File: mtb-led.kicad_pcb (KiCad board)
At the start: 2 copper layers, 120 x 50 mm, 60 parts, among them J7 AVR-ISP-6, J9 DEBUG, SW1 SW_Push, U1 ATmega328PB-A, U2 78M05, U3 TLC5940PWP, U4 TLC5940PWP, U5 MAX487E, Y1 14.7456 MHz

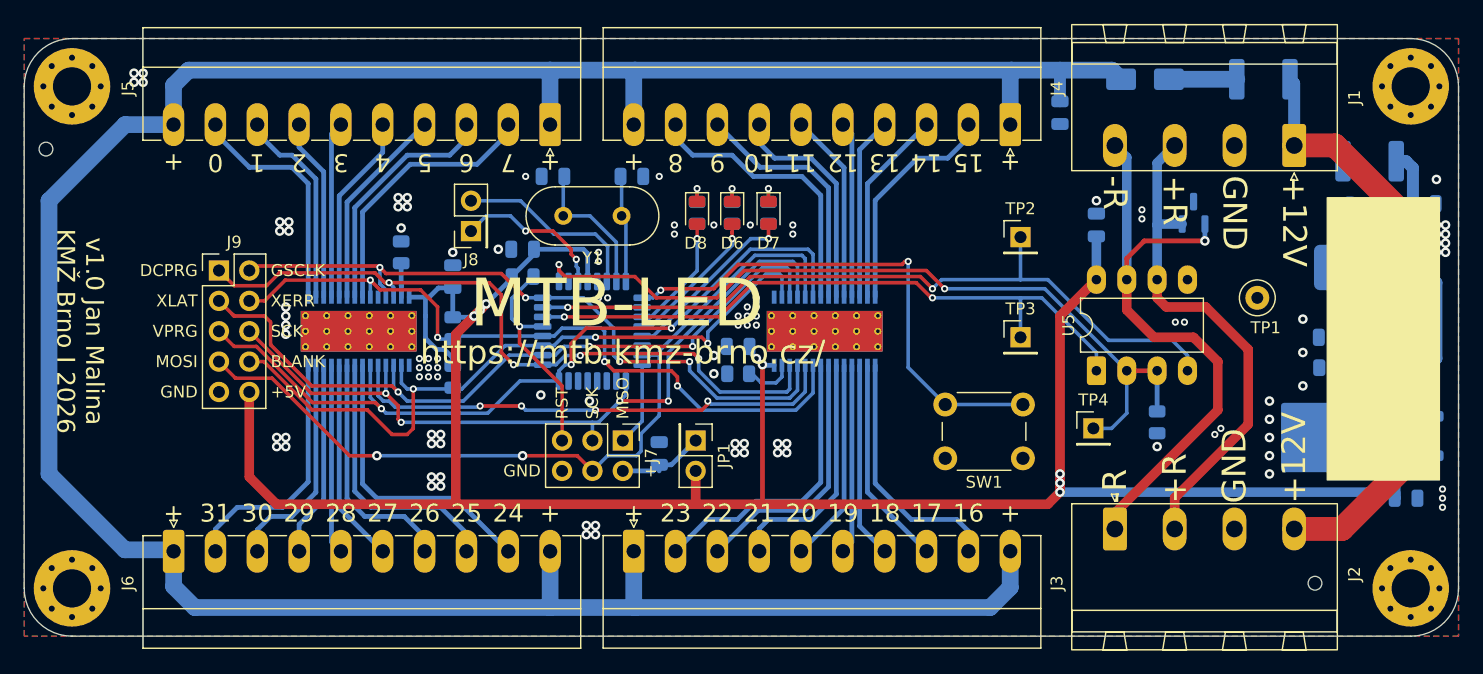
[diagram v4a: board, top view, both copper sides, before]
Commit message: Tweak silkscreen.
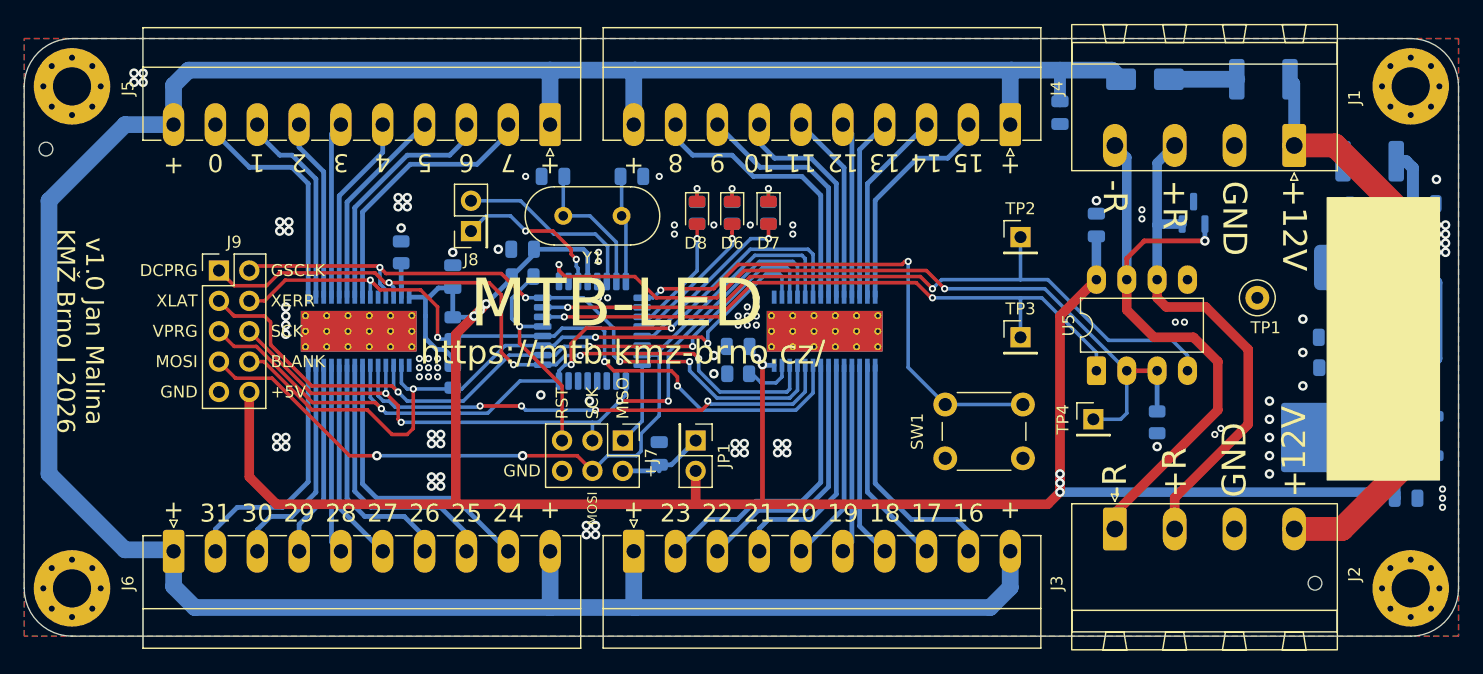
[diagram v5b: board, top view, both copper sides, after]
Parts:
- Y1: footprint Crystal:Crystal_HC49-U_Vertical -> Crystal:Crystal_HC49-4H_Vertical
- moved TP4 0.76 mm to (171.4, 101.9)
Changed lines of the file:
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@@
 	(footprint "Connector_PinHeader_2.54mm:PinHeader_1x01_P2.54mm_Vertical"
 		(layer "F.Cu")
-		(at 171.45 102.616)
+		(at 171.45 101.854)
 		(descr "Through hole straight pin header, 1x01, 2.54mm pitch, single row")
 		(tags "Through hole pin header THT 1x01 2.54mm single row")
 		(property "Reference" "TP4"
-			(at 0 -2.38 0)
+			(at -2.55 0 90)
 			(layer "F.SilkS")
 			(effects
@@
 		)
 	)
-	(footprint "Crystal:Crystal_HC49-U_Vertical"
+	(footprint "Crystal:Crystal_HC49-4H_Vertical"
 		(layer "F.Cu")
 		(at 131.98 84.836 180)
-		(descr "HC-49/U, Crystal, http://5hertz.com/pdfs/04404_D.pdf")
+		(descr "HC-49-4H, Crystal, http://5hertz.com/pdfs/04404_D.pdf")
 		(property "Reference" "Y1"
-			(at 2.44 -3.52 0)
+			(at 2.44 -3.52 180)
 			(layer "F.SilkS")
 			(effects
@@
 		)
 		(property "Value" "14.7456 MHz"
-			(at 2.44 3.52 0)
+			(at 2.44 3.52 180)
 			(layer "F.Fab")
 			(effects
@@
 		)
 		(property "Datasheet" ""
-			(at 0 0 0)
+			(at 0 0 180)
 			(layer "F.Fab")
 			(hide yes)
@@
 		)
 		(property "Description" "Two pin crystal"
-			(at 0 0 0)
+			(at 0 0 180)
 			(layer "F.Fab")
 			(hide yes)
@@
 		(attr through_hole)
 		(fp_line
-			(start 5.565 2.435)
-			(end -0.685 2.435)
+			(start 5.64 2.435)
+			(end -0.76 2.435)
 			(stroke
 				(width 0.12)
@@
 		)
 		(fp_line
-			(start -0.685 -2.435)
-			(end 5.565 -2.435)
+			(start -0.76 -2.435)
+			(end 5.64 -2.435)
 			(stroke
 				(width 0.12)
@@
 		)
 		(fp_arc
-			(start 5.565 -2.435)
-			(mid 8 0)
-			(end 5.565 2.435)
+			(start 5.64 -2.435)
+			(mid 8.075 0)
+			(end 5.64 2.435)
 			(stroke
 				(width 0.12)
@@
 		)
 		(fp_arc
-			(start -0.685 2.435)
-			(mid -3.12 0)
-			(end -0.685 -2.435)
+			(start -0.76 2.435)
+			(mid -3.195 0)
+			(end -0.76 -2.435)
 			(stroke
 				(width 0.12)
@@
 		)
 		(fp_line
-			(start 5.56 2.83)
-			(end -0.68 2.83)
+			(start 5.64 2.83)
+			(end -0.76 2.83)
 			(stroke
 				(width 0.05)
@@
 		)
 		(fp_line
-			(start -0.68 -2.83)
-			(end 5.56 -2.83)
+			(start -0.76 -2.83)
+			(end 5.64 -2.83)
 			(stroke
 				(width 0.05)
@@
 		)
 		(fp_arc
-			(start 5.56 -2.83)
-			(mid 8.39 0)
-			(end 5.56 2.83)
+			(start 5.64 -2.83)
+			(mid 8.47 0)
+			(end 5.64 2.83)
 			(stroke
 				(width 0.05)
@@
 		)
 		(fp_arc
-			(start -0.68 2.83)
-			(mid -3.51 0)
-			(end -0.68 -2.83)
+			(start -0.76 2.83)
+			(mid -3.59 0)
+			(end -0.76 -2.83)
 			(stroke
 				(width 0.05)
@@
 		)
 		(fp_line
-			(start 5.565 2.325)
-			(end -0.685 2.325)
+			(start 5.64 2.325)
+			(end -0.76 2.325)
 			(stroke
 				(width 0.1)
@@
 		)
 		(fp_line
-			(start -0.685 -2.325)
-			(end 5.565 -2.325)
+			(start -0.76 -2.325)
+			(end 5.64 -2.325)
 			(stroke
 				(width 0.1)
@@
 		)
 		(fp_arc
-			(start 5.565 -2.325)
-			(mid 7.89 0)
-			(end 5.565 2.325)
+			(start 5.64 -2.325)
+			(mid 7.965 0)
+			(end 5.64 2.325)
 			(stroke
 				(width 0.1)
@@
 		)
 		(fp_arc
-			(start -0.685 2.325)
-			(mid -3.01 0)
-			(end -0.685 -2.325)
+			(start -0.76 2.325)
+			(mid -3.085 0)
+			(end -0.76 -2.325)
 			(stroke
 				(width 0.1)
@@
 		)
 		(fp_text user "${REFERENCE}"
-			(at 2.44 0 0)
+			(at 2.44 0 180)
 			(layer "F.Fab")
 			(effects
@@
 		)
 		(embedded_fonts no)
-		(model "${KICAD9_3DMODEL_DIR}/Crystal.3dshapes/Crystal_HC49-U_Vertical.step"
+		(model "${KICAD9_3DMODEL_DIR}/Crystal.3dshapes/Crystal_HC49-4H_Vertical.step"
 			(offset
 				(xyz 0 0 0)
@@
 		(tags "tact sw push 6mm")
 		(property "Reference" "SW1"
-			(at 3.25 -2 0)
+			(at 8.838 2.25 90)
 			(layer "F.SilkS")
 			(effects
@@
 	)
 	(gr_text "+12V"
-		(at 188.25 81.45 270)
+		(at 188.25 81.8 270)
 		(layer "F.SilkS")
 		(effects
@@
 		)
 	)
+	(gr_text "MOSI"
+		(at 129.54 107.9 90)
+		(layer "F.SilkS")
+		(effects
+			(font
+				(size 0.8 0.8)
+				(thickness 0.1)
+			)
+			(justify right)
+		)
+	)
 	(gr_text "4"
 		(at 112 79.5 180)
@@
 	)
 	(gr_text "-R"
-		(at 173.25 108.9 90)
+		(at 173.25 108.4205 90)
 		(layer "F.SilkS")
 		(effects
@@
 	)
 	(gr_text "+"
-		(at 126 110.6 0)
+		(at 126 110.3 0)
 		(layer "F.SilkS")
 		(effects
@@
 	)
 	(gr_text "+R"
-		(at 178.25 108.9 90)
+		(at 178.25 108.4 90)
 		(layer "F.SilkS")
 		(effects
@@
 	)
 	(gr_text "-R"
-		(at 173.25 81.45 270)
+		(at 173.25 81.8 270)
 		(layer "F.SilkS")
 		(effects
@@
 	)
 	(gr_text "+"
-		(at 132.995 79.5 180)
+		(at 132.995 79.8 180)
 		(layer "F.SilkS")
 		(effects
@@
 	)
 	(gr_text "GND"
-		(at 183.25 108.9 90)
+		(at 183.25 108.4 90)
 		(layer "F.SilkS")
 		(effects
@@
 	)
 	(gr_text "+"
-		(at 164.5 110.6 0)
+		(at 164.5 110.3 0)
 		(layer "F.SilkS")
 		(effects
@@
 	)
 	(gr_text "+"
-		(at 94.5 110.6 0)
+		(at 94.5 110.3 0)
 		(layer "F.SilkS")
 		(effects
@@
 	)
 	(gr_text "+12V"
-		(at 188.25 108.9 90)
+		(at 188.25 108.4 90)
 		(layer "F.SilkS")
 		(effects
@@
 	)
 	(gr_text "+"
-		(at 94.5 79.5 180)
+		(at 94.5 79.8 180)
 		(layer "F.SilkS")
 		(effects
@@
 	)
 	(gr_text "GND"
-		(at 183.25 81.45 270)
+		(at 183.25 81.9 270)
 		(layer "F.SilkS")
 		(effects
@@
 	)
 	(gr_text "+R"
-		(at 178.25 81.45 270)
+		(at 178.25 81.8 270)
 		(layer "F.SilkS")
 		(effects
@@
 	)
 	(gr_text "+"
-		(at 164.495 79.5 180)
+		(at 164.5 79.8 180)
 		(layer "F.SilkS")
 		(effects
@@
 	)
 	(gr_text "+"
-		(at 126 79.5 180)
+		(at 125.994 79.8 180)
 		(layer "F.SilkS")
 		(effects
@@
 	)
 	(gr_text "+"
-		(at 133 110.6 0)
+		(at 132.994 110.2915 0)
 		(layer "F.SilkS")
 		(effects
@@
 	)
 	(segment
-		(start 172.974 102.616)
-		(end 171.45 102.616)
-		(width 0.3)
-		(layer "B.Cu")
-		(net 67)
-	)
-	(segment
 		(start 167.386 90.932)
 		(end 174.244 97.79)
@@
 	)
 	(segment
-		(start 174.244 101.346)
-		(end 172.974 102.616)
+		(start 173.736 101.854)
+		(end 171.45 101.854)
 		(width 0.3)
 		(layer "B.Cu")
@@
 		(width 0.3)
 		(layer "B.Cu")
+		(net 67)
+	)
+	(segment
+		(start 174.244 101.346)
+		(end 173.736 101.854)
+		(width 0.3)
+		(layer "B.Cu")

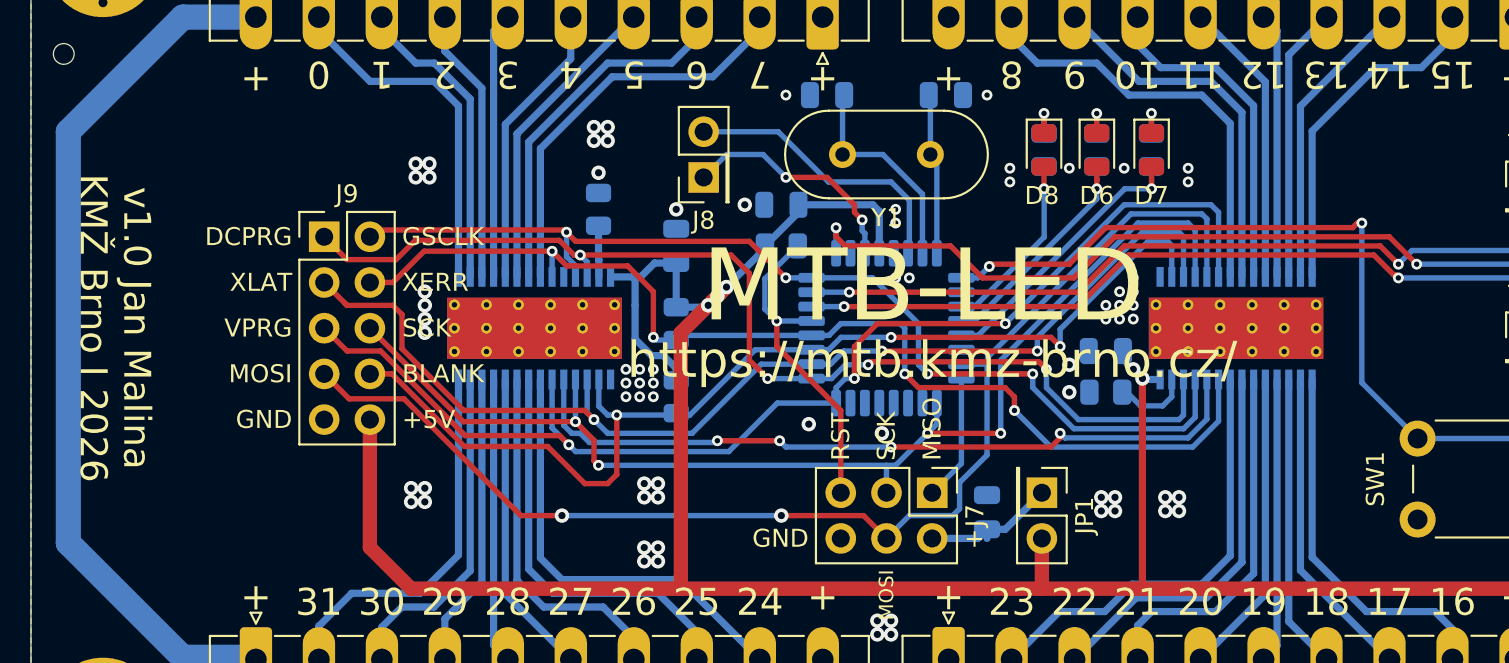
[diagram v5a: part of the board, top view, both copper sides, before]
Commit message: Rewire MCU connection (v1.1).
* Use OCR1A/B pins for XLAT & BLANK. HW timer output required.
* Reconnect BLUE LED to different PIN.
* Add MISO TLC->ATmega.
* Use SPI1 for TLS connection, SPI0 for programming.
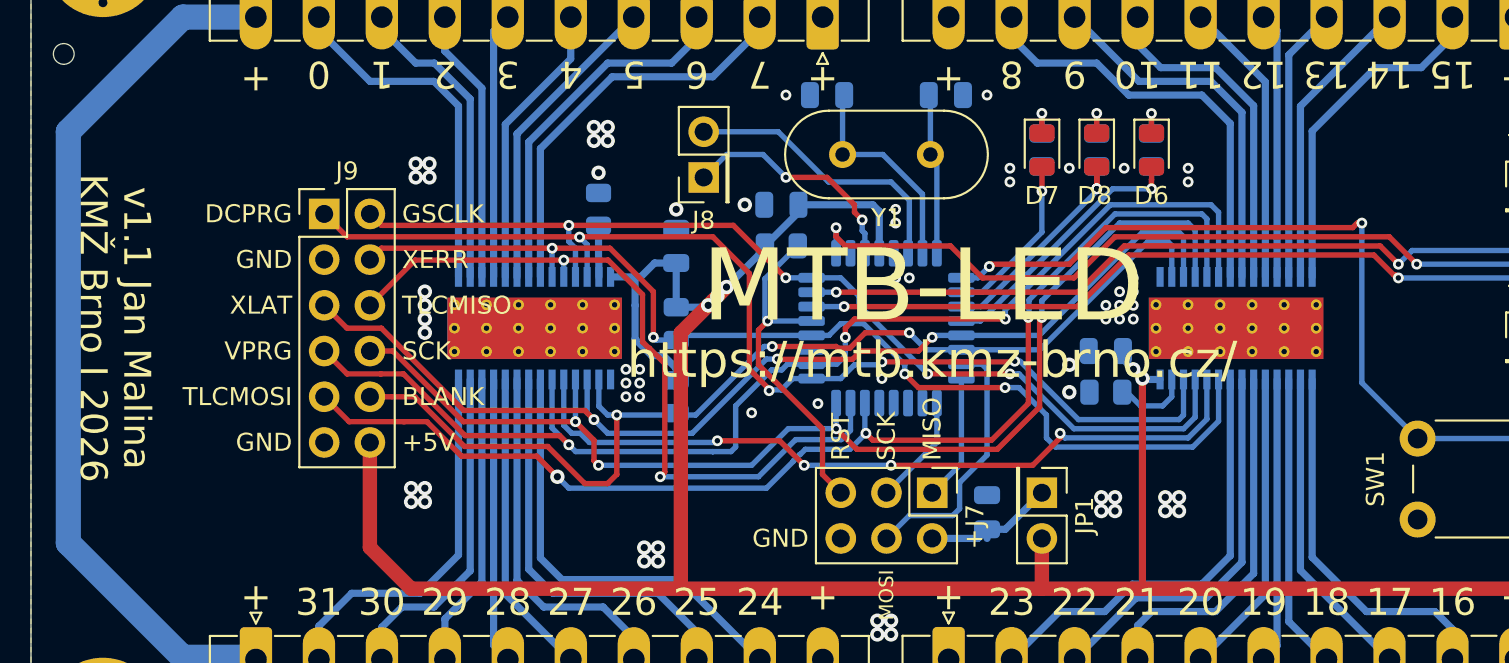
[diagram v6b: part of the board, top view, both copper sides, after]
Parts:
- J9: footprint Connector_PinHeader_2.54mm:PinHeader_2x05_P2.54mm_Vertical -> Connector_PinHeader_2.54mm:PinHeader_2x06_P2.54mm_Vertical
- moved R8 6.09 mm to (138.2, 84.6)
- moved D7 6.09 mm to (138.2, 84.6)
- moved R7 3.04 mm to (144.3, 84.6)
- moved D6 3.04 mm to (144.3, 84.6)
- moved D8 2.93 mm to (141.2, 84.6)
- moved R6 2.93 mm to (141.2, 84.6)
- moved J9 1.27 mm to (98.3, 88.1)
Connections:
- J9 pad 10: +5V -> /BLANK
- J9 pad 3: /XLAT -> GND
- J9 pad 5: /VPRG -> /XLAT
- J9 pad 6: /SCK -> /TLCMISO
- J9 pad 7: /MOSI -> /VPRG
- J9 pad 8: /BLANK -> /TLCSCK
- J9 pad 9: GND -> /TLCMOSI
- U1 pad 10: unconnected-(U1-PD6-Pad10) -> /LED_BLUE
- U1 pad 13: /LED_BLUE -> /XLAT
- U1 pad 14: unconnected-(U1-PB2-Pad14) -> /BLANK
- U1 pad 22: unconnected-(U1-PE3-Pad22) -> /TLCMOSI
- U1 pad 23: unconnected-(U1-PC0-Pad23) -> /TLCMISO
- U1 pad 24: /VPRG -> /TLCSCK
- U1 pad 26: /XLAT -> /VPRG
- U1 pad 27: /BLANK -> unconnected-(U1-PC4-Pad27)
- U3 pad 4: /SCK -> /TLCSCK
- U3 pad 5: /MOSI -> /TLCMOSI
- U4 pad 24: unconnected-(U4-SOUT-Pad24) -> /TLCMISO
- U4 pad 4: /SCK -> /TLCSCK
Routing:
- net /TLCMOSI: track 0.00 -> 66.2 mm, vias 0 -> 3
- net /TLCSCK: track 0.00 -> 65.6 mm, vias 0 -> 4
- net /SCK: track 66.2 -> 6.14 mm, vias 4 -> 0
- net /MOSI: track 69.1 -> 14.7 mm, vias 2 -> 0
- net /TLCMISO: track 0.00 -> 41.8 mm, vias 0 -> 2
- net /LED_BLUE: track 15.2 -> 9.48 mm
- net /LED_GREEN: track 12.1 -> 14.8 mm
- net /LED_RED: track 10.1 -> 12.8 mm, vias 1 -> 2
- net /XLAT: track 62.3 -> 60.1 mm
- net +5V: track 201.5 -> 200.2 mm
- net /XERR: track 60.9 -> 59.7 mm
- net /DCPRG: track 60.5 -> 61.5 mm
- net /GSCLK: track 57.4 -> 56.5 mm
- net /RST: track 18.2 -> 19.1 mm
- net Net-(U3-SOUT): track 42.1 -> 43.0 mm
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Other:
- board text added: "TLCMISO"
- board text added: "TLCMOSI"
- board text added: "v1.1 Jan Malina KMŽ Brno I 2026"
- board text removed: "v1.0 Jan Malina KMŽ Brno I 2026"

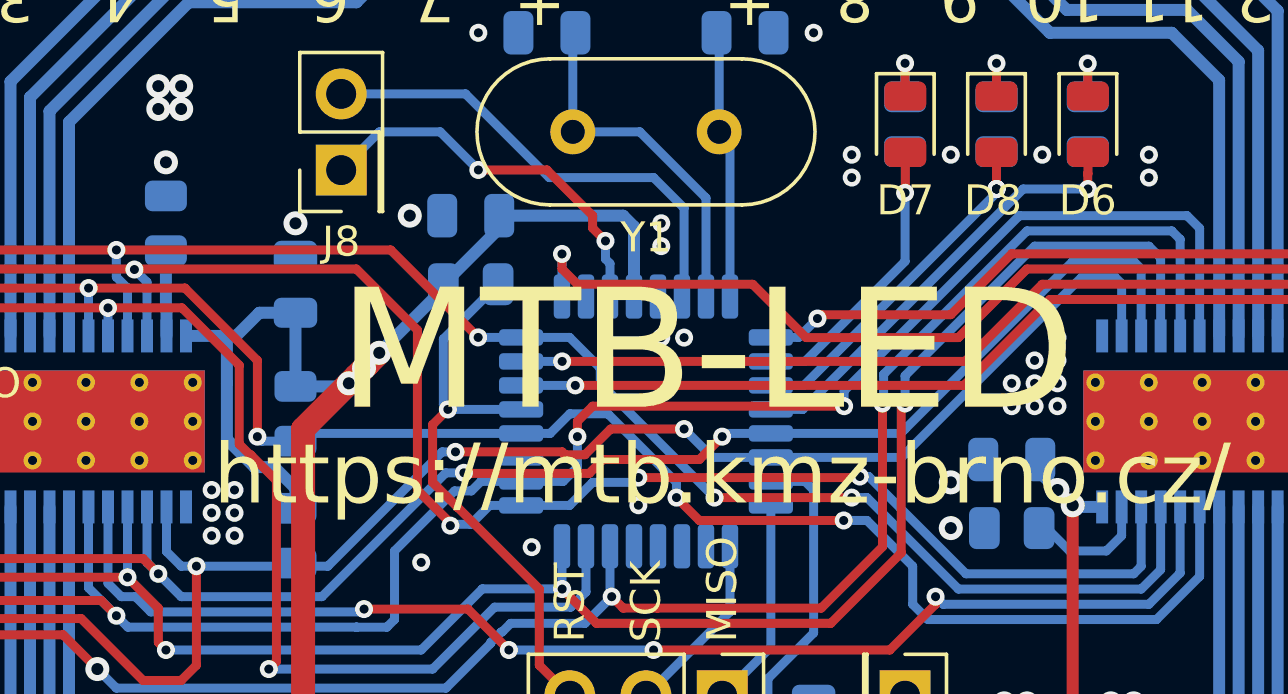
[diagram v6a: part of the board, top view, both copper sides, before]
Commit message: Connect TLC5940 thermal pad to GND.
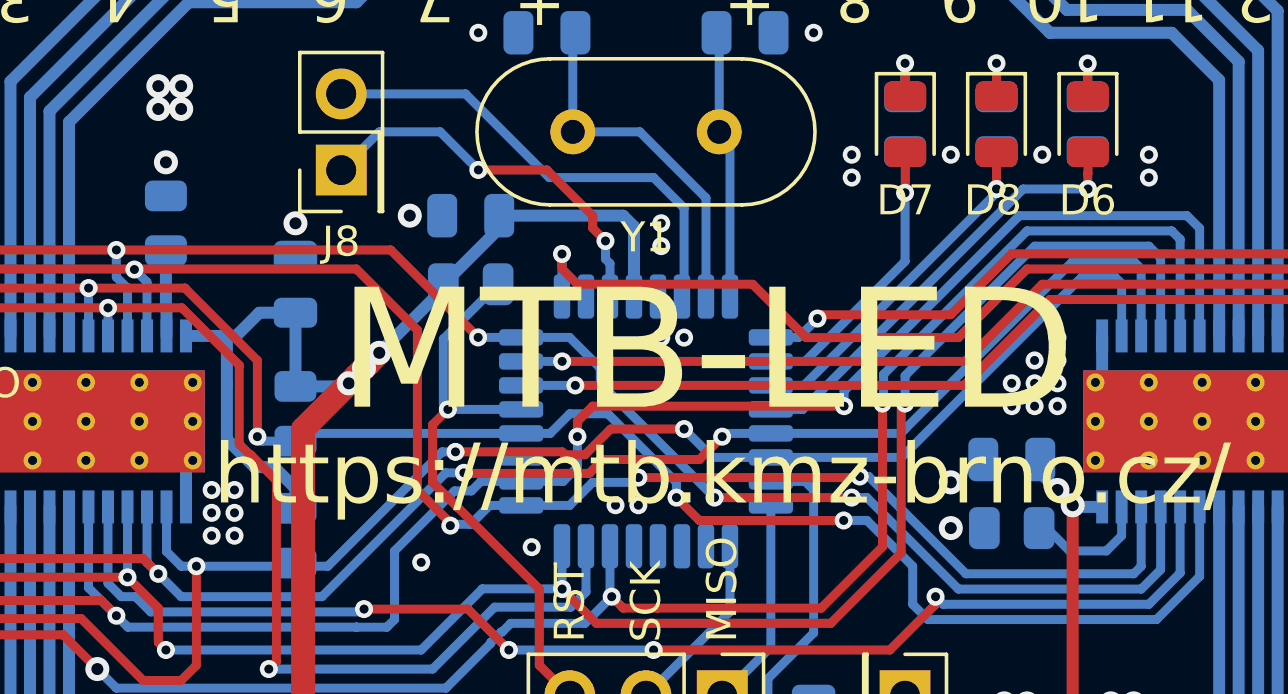
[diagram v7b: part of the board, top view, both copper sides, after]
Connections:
- U3 pad 29: unconnected-(U3-PAD-Pad29)_5 -> GND
- U4 pad 29: unconnected-(U4-PAD-Pad29)_4 -> GND
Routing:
- net GND: track 0.00 -> 3.29 mm, vias 105 -> 106
- net /LED_RED: vias 2 -> 1

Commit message: PCB updates.
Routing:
- net /DCPRG: track 61.5 -> 63.3 mm
- net /RST: track 19.1 -> 20.3 mm
- net GND: track 3.29 -> 3.92 mm, vias 106 -> 119
